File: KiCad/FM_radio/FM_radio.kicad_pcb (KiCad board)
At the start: 2 copper layers, 33 x 48 mm, 77 parts, among them IC1 MCP73831T-2ACI_OT, IC2 SI4703-C19-GM, IC3 TPA741DR, IC4 TPA6111A2DR, J1 UJC-HP2-3-SMT-TR, J2 Conn_01x06_Pin, J3 SJ2-35853A-SMT-TR, U1 ATmega328P-A, Y1 ABS06N-32.768kHz-T

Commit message: Text (J2 silkscreen)
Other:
- board text added: "SCK MISO MOSI RST 3v3 GND"
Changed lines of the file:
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@@
 		(tags "Through hole pin header THT 1x06 1.27mm single row")
 		(property "Reference" "J2"
-			(at 0.025 8.14 180)
+			(at 0 -2.21 180)
 			(layer "F.SilkS")
 			(effects
@@
 		(layer "Edge.Cuts")
 	)
+	(gr_text "SCK\nMISO\nMOSI\nRST\n3v3\nGND"
+		(at 120.6 105.35 0)
+		(layer "F.SilkS")
+		(effects
+			(font
+				(size 1 1)
+				(thickness 0.15)
+			)
+			(justify left bottom)
+		)
+	)
 	(segment

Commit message: Display flip update
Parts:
- moved Cpmp1 24.6 mm to (124.5, 86.5), turned to -90 degrees
- moved Ccom1 24.0 mm to (150.3, 92.0)
- moved Cb5 22.7 mm to (148.6, 84.2)
- moved Cpmp2 19.5 mm to (127.8, 83.2), turned to 0 degrees
- moved Cs3 19.2 mm to (132.0, 83.1), turned to 0 degrees
- moved Rref1 8.02 mm to (144.2, 83.3)
- moved Cs4 5.27 mm to (136.1, 83.1)
- moved Cxtl2 5.26 mm to (127.1, 80.5), turned to 180 degrees
- moved Cb6 0.69 mm to (126.3, 89.7), turned to 0 degrees
- moved Rin3 0.52 mm to (123.2, 92.2)
- moved Y1 0.45 mm to (131.8, 80.5)
- moved Cant1 0.39 mm to (121.8, 81.5)
- moved Lant1 0.35 mm to (121.8, 85.9)
- moved Cin5 0.30 mm to (129.2, 81.1)
- moved Cxtl1 0.25 mm to (136.1, 80.2)
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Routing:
- net /Vbat: track 91.2 -> 106.0 mm, vias 9 -> 10
- net /3v3: track 92.7 -> 102.5 mm, vias 1 -> 2
- net Net-(OLED1-VCOMH): track 4.50 -> 11.1 mm
- net Net-(OLED1-VCC): track 4.55 -> 10.8 mm
- net /GPIO2: track 20.6 -> 26.8 mm
- net /SCL: track 49.8 -> 45.4 mm, vias 1 -> 3
- net Net-(OLED1-IREF): track 7.52 -> 3.53 mm
- net GND: track 15.1 -> 18.7 mm, vias 38 -> 64
- net /RST2: track 52.8 -> 55.7 mm
- net Net-(OLED1-C1P): track 6.93 -> 4.08 mm
- net /ROUT: track 29.3 -> 26.7 mm
- net /XTAL2: track 13.0 -> 11.0 mm
- net Net-(OLED1-C2P): track 7.17 -> 5.26 mm
- net /SDA: track 46.8 -> 48.4 mm, vias 3 -> 1
- net Net-(OLED1-C1N): track 5.28 -> 3.89 mm
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
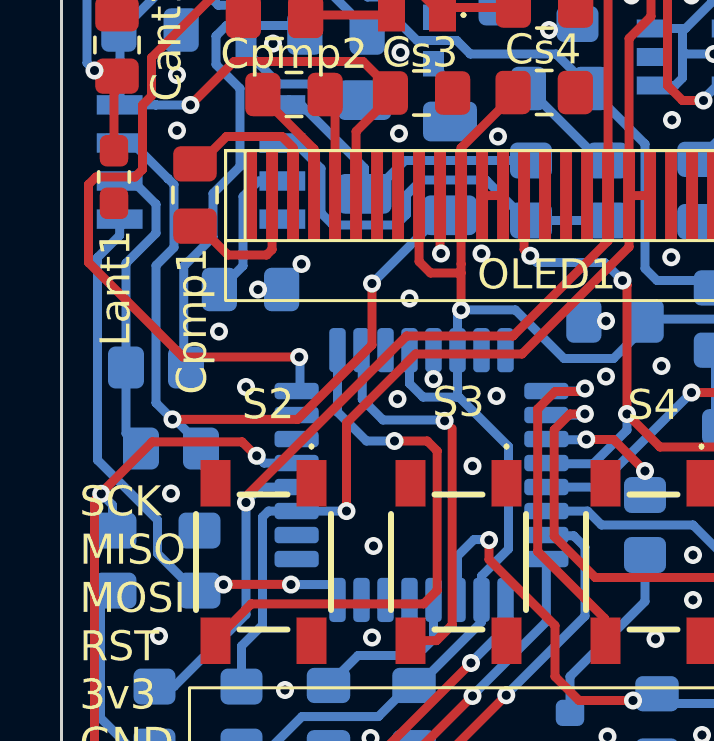
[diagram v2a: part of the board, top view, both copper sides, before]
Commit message: TPA6111 VO2 route
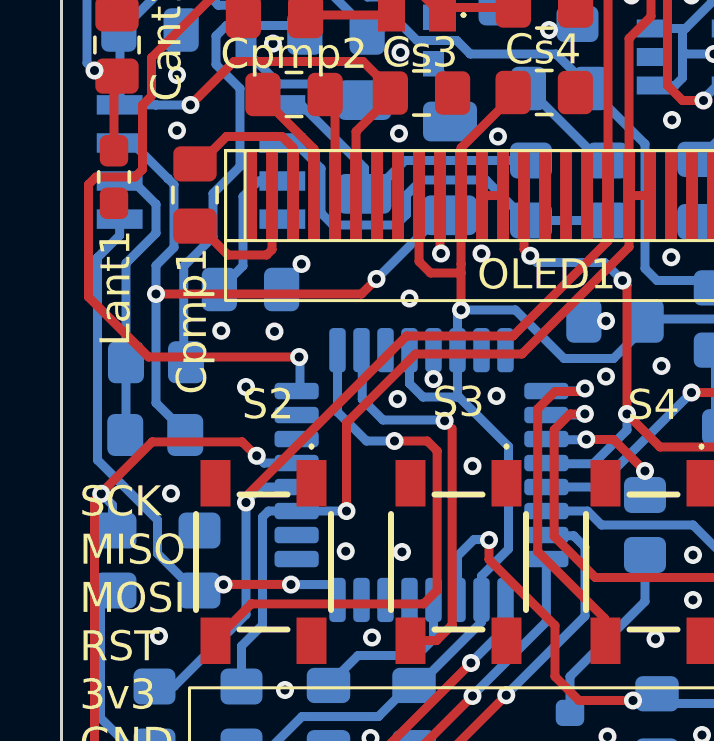
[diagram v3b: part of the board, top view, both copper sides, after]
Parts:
- moved Rfb3 0.69 mm to (123.1, 94.5)
- moved Rin3 0.17 mm to (123.2, 92.1)
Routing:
- net Net-(IC4-VO2): track 26.0 -> 22.8 mm
- net Net-(IC4-IN2-): track 11.1 -> 10.1 mm
- net /GPIO2: track 26.8 -> 27.5 mm
- net GND: vias 64 -> 65

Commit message: Minor changes
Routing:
- net Net-(J3-RING): track 11.5 -> 10.9 mm
- net GND: vias 65 -> 70

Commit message: Lant added
Last changes before JLC PCB
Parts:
- added Lant2: 350n, Inductor_SMD:L_0805_2012Metric_Pad1.15x1.40mm_HandSolder, F.Cu at (123.8, 75.5)
- turned Cc1 to 90 degrees
- turned Cc2 to 90 degrees
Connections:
- AE1 pad 1: /ANT -> Net-(AE1-A)
- Cc1 pad 1: Net-(Cc1-Pad1) -> Net-(IC4-VO1)
- Cc1 pad 2: Net-(IC4-VO1) -> Net-(Cc1-Pad2)
- Cc2 pad 1: Net-(Cc2-Pad1) -> Net-(IC4-VO2)
- Cc2 pad 2: Net-(IC4-VO2) -> Net-(Cc2-Pad2)
- Dant1 pad 2: /ANT -> Net-(AE1-A)
- FB1 pad 1: Net-(Cc1-Pad1) -> Net-(Cc1-Pad2)
- FB2 pad 2: Net-(Cc2-Pad1) -> Net-(Cc2-Pad2)
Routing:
- net /ANT: track 16.7 -> 9.06 mm
- net Net-(AE1-A): track 0.00 -> 5.58 mm
- net Net-(Cc1-Pad2): track 0.00 -> 4.83 mm
- net Net-(Cc1-Pad1): track 4.83 -> 0.00 mm
- net Net-(Cc2-Pad2): track 0.00 -> 2.46 mm
- net Net-(Cc2-Pad1): track 2.46 -> 0.00 mm
- net GND: vias 70 -> 71
